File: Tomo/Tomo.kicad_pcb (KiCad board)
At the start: 2 copper layers, 35.6 x 55.9 mm, 60 parts, among them J001 USB_MICROB, J002 STANDOFF_GND, J006 USB_MICROB, J101 Raspberry_Pi_1, J102 CONN_01X02, J301 CONN_02X03, J401 CONN_01X04, U001 FT232RL, U301 ADuM3221, U401 ATMEGA328P-AU, U501 MPU9250, U601 FGPMMOPA6H, U701 HMC5883L, U801 BMP180, U901 L3G4200D, X611 uFL, Y407 16MHz

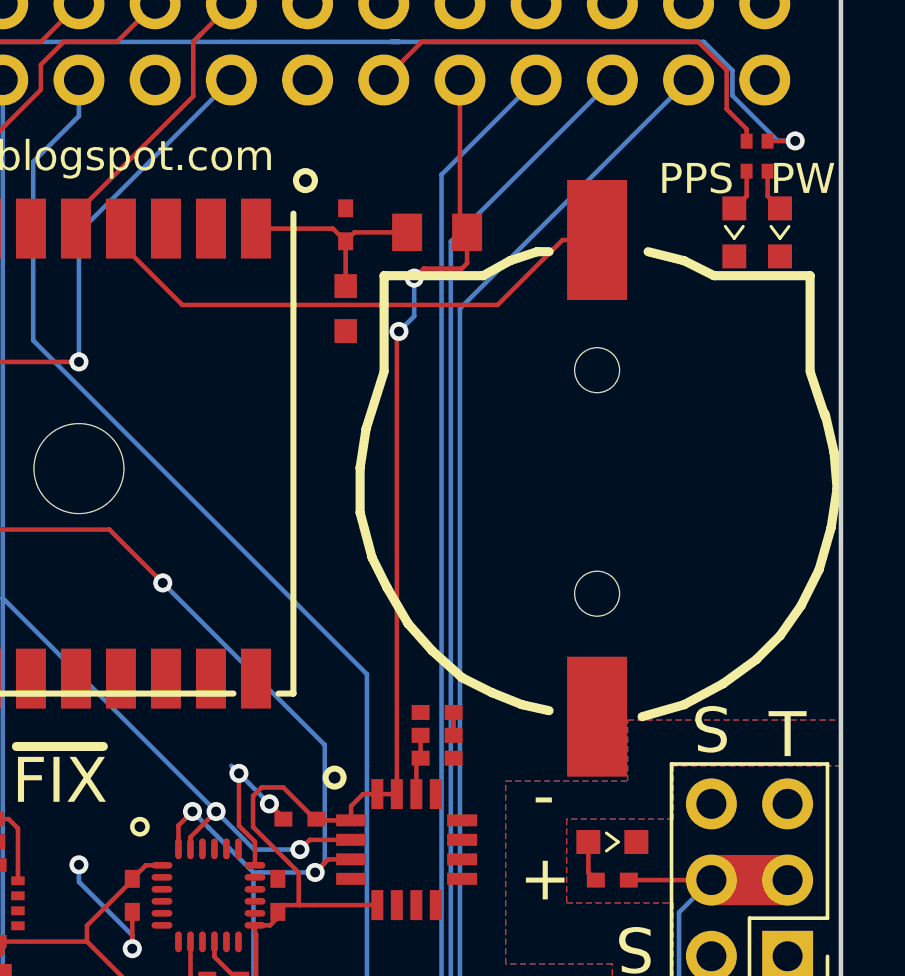
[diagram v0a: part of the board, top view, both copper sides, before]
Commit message: Adding supercap
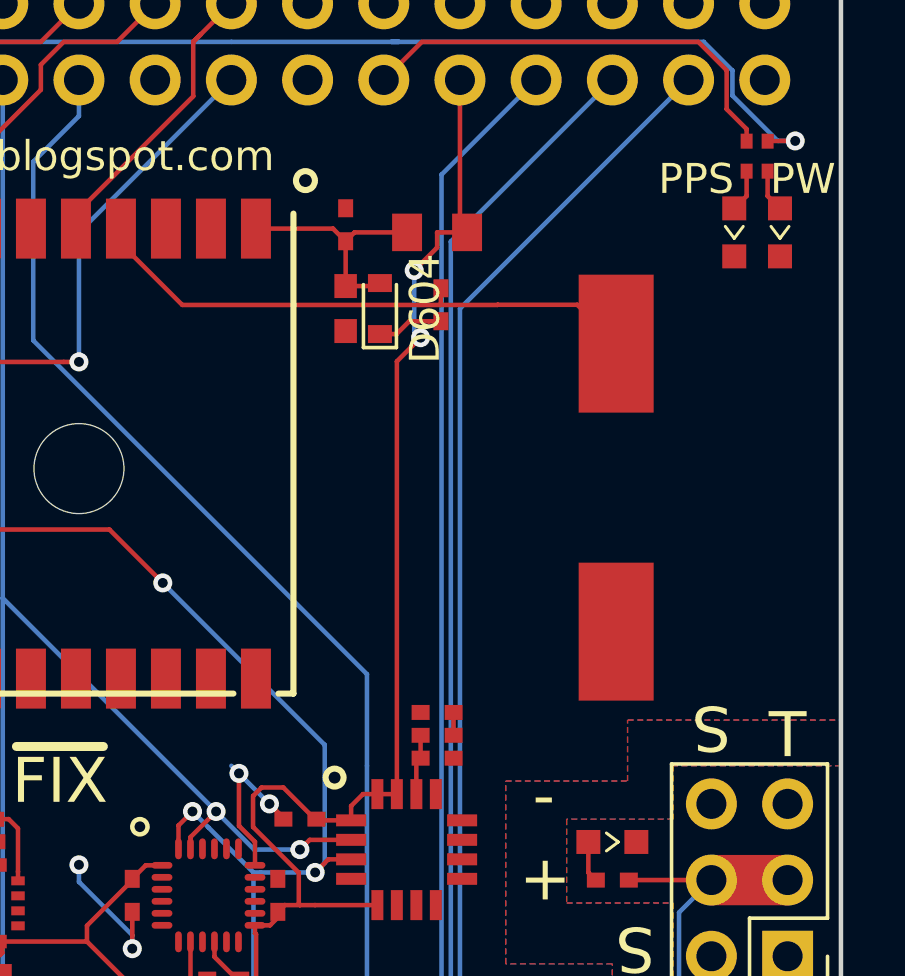
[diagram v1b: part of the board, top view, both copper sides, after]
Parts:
- removed B603: Coin_Cell, KwanSystems:CR1220-2
- added C604: 220mF, KwanSystems:Supercap, F.Cu at (154.6, 117.3)
- added D604: D_Schottky, Diodes_SMD:D_0603, F.Cu at (146.7, 111.3)
- added R604: 10k, KwanSystems:SMD_0402, F.Cu at (148.7, 111.2)
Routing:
- net Net-(D604-Pad1): track 0.00 -> 2.21 mm
- net /VGPS: track 6.83 -> 8.01 mm
- net /VBACKUP: track 18.1 -> 18.9 mm

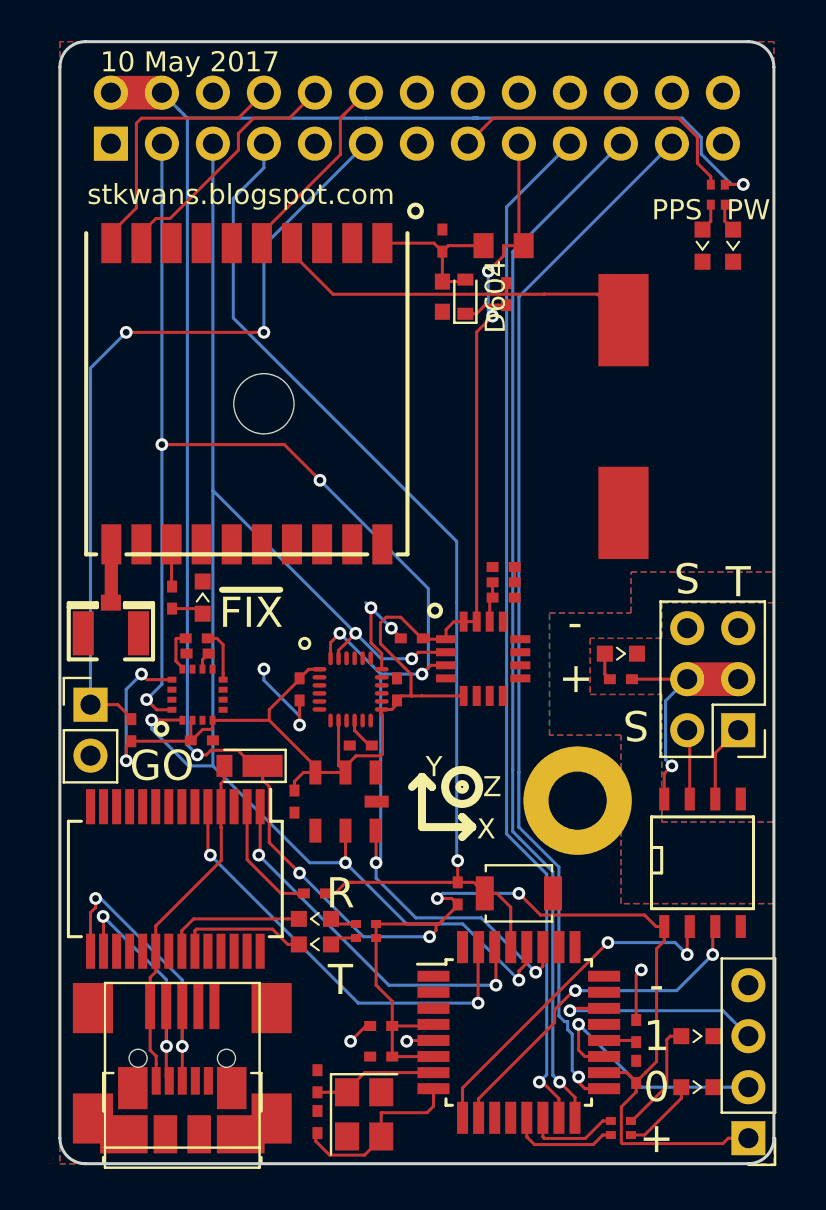
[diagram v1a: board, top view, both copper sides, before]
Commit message: Broke the schematic down to a bunch of subsheets
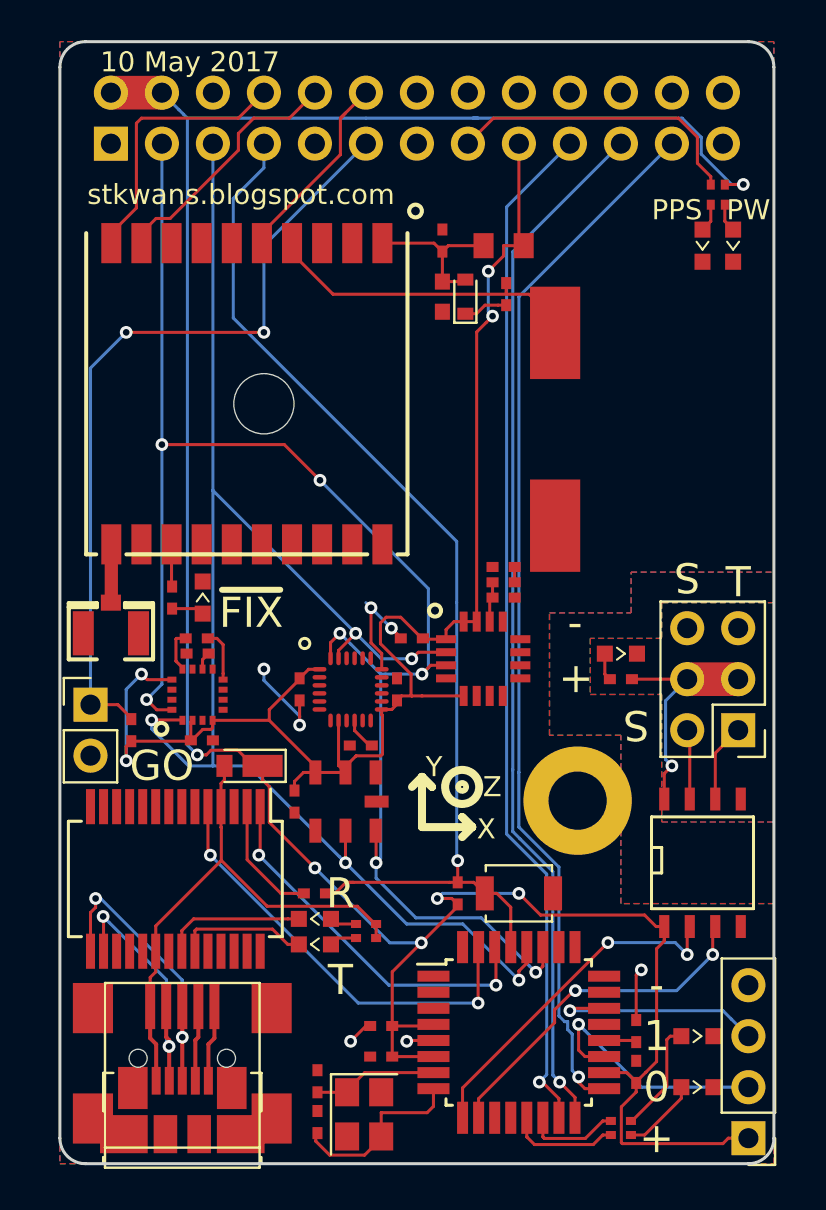
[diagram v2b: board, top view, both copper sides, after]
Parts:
- removed J006: USB_MICROB, KwanSystems:USB_Mini-B
- J001: footprint KwanSystems:USB_Micro-B_Molex_47346-0001 -> KwanSystems:USB_Double-B
- moved C604 3.46 mm to (151.2, 117.9)
- moved J001 2.79 mm to (132.6, 154.5)
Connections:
- net /ANT renamed /UltimateGPS/ANT
- net /AREF renamed /Arduino/AREF
- net /C1 renamed /HMC5883L/C1
- net /D+ renamed /Arduino/D+
- net /D- renamed /Arduino/D-
- net /D0/RX renamed /Arduino/D0
- net /D1/TX renamed /Arduino/D1
- net /DTR renamed /Arduino/DTR
- net /PLLFILT renamed /L3G4200D/PLLFILT
- net /PLLFILT- renamed /L3G4200D/PLLFILT-
- net /RXLED renamed /Arduino/RXLED
- net /RXLED+ renamed /Arduino/RXLED+
- net /SETC renamed /HMC5883L/SETC
- net /SETP renamed /HMC5883L/SETP
- net /TXLED renamed /Arduino/TXLED
- net /TXLED+ renamed /Arduino/TXLED+
- net /VBACKUP renamed /UltimateGPS/VBACKUP
- net /VGPS renamed /UltimateGPS/VGPS
- net /XTAL1 renamed /Arduino/XTAL1
- net /XTAL2 renamed /Arduino/XTAL2
- J001 pad 4: (no net) -> Net-(J001-Pad4)
- J101 pad 1: (no net) -> Net-(J101-Pad1)
- J101 pad 13: (no net) -> Net-(J101-Pad13)
- J101 pad 16: (no net) -> Net-(J101-Pad16)
- J101 pad 18: (no net) -> Net-(J101-Pad18)
- J101 pad 22: (no net) -> Net-(J101-Pad22)
- J101 pad 24: (no net) -> Net-(J101-Pad24)
- J101 pad 26: (no net) -> Net-(J101-Pad26)
- R022 pad 1: +5V -> /VBUS
- R022 pad 2: +5V -> /VBUS
- U001 pad 10: (no net) -> Net-(U001-Pad10)
- U001 pad 11: (no net) -> Net-(U001-Pad11)
- U001 pad 12: (no net) -> Net-(U001-Pad12)
- U001 pad 13: (no net) -> Net-(U001-Pad13)
- U001 pad 14: (no net) -> Net-(U001-Pad14)
- U001 pad 17: (no net) -> Net-(U001-Pad17)
- U001 pad 19: (no net) -> Net-(U001-Pad19)
- U001 pad 27: (no net) -> Net-(U001-Pad27)
- U001 pad 28: (no net) -> Net-(U001-Pad28)
- U001 pad 3: (no net) -> Net-(U001-Pad3)
- U001 pad 6: (no net) -> Net-(U001-Pad6)
- U001 pad 9: (no net) -> Net-(U001-Pad9)
- U401 pad 1: (no net) -> /Arduino/D3
- U401 pad 11: (no net) -> /Arduino/D7
- U401 pad 12: (no net) -> /Arduino/D8
- U401 pad 2: (no net) -> /Arduino/D4
- U401 pad 23: (no net) -> /Arduino/A0
- U401 pad 24: (no net) -> /Arduino/A1
- U401 pad 25: (no net) -> /Arduino/A2
- U401 pad 26: (no net) -> /Arduino/A3
- U401 pad 32: (no net) -> /Arduino/D2
- U501 pad 11: (no net) -> Net-(U501-Pad11)
- U501 pad 12: (no net) -> Net-(U501-Pad12)
- U501 pad 7: (no net) -> Net-(U501-Pad7)
- U601 pad 14: (no net) -> Net-(U601-Pad14)
- U601 pad 2: (no net) -> Net-(U601-Pad2)
- U701 pad 15: (no net) -> Net-(U701-Pad15)
- U901 pad 6: (no net) -> Net-(U901-Pad6)
- U901 pad 7: (no net) -> Net-(U901-Pad7)
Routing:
- net /VBUS: track 17.4 -> 27.1 mm
- net +5V: track 134.4 -> 130.1 mm
- net Net-(J001-Pad4): track 0.00 -> 3.78 mm
- net /UltimateGPS/VBACKUP: track 18.9 -> 17.3 mm

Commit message: j
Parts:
- added B604: Coin_Cell, KwanSystems:CR1220-2, F.Cu at (154.1, 117.4)
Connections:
- J101 pad 1: Net-(J101-Pad1) -> (no net)
- J101 pad 13: Net-(J101-Pad13) -> (no net)
- J101 pad 16: Net-(J101-Pad16) -> (no net)
- J101 pad 18: Net-(J101-Pad18) -> (no net)
- J101 pad 22: Net-(J101-Pad22) -> (no net)
- J101 pad 24: Net-(J101-Pad24) -> (no net)
- J101 pad 26: Net-(J101-Pad26) -> (no net)
- U001 pad 10: Net-(U001-Pad10) -> (no net)
- U001 pad 11: Net-(U001-Pad11) -> (no net)
- U001 pad 12: Net-(U001-Pad12) -> (no net)
- U001 pad 13: Net-(U001-Pad13) -> (no net)
- U001 pad 14: Net-(U001-Pad14) -> (no net)
- U001 pad 17: Net-(U001-Pad17) -> (no net)
- U001 pad 19: Net-(U001-Pad19) -> (no net)
- U001 pad 27: Net-(U001-Pad27) -> (no net)
- U001 pad 28: Net-(U001-Pad28) -> (no net)
- U001 pad 3: Net-(U001-Pad3) -> (no net)
- U001 pad 6: Net-(U001-Pad6) -> (no net)
- U001 pad 9: Net-(U001-Pad9) -> (no net)
- U401 pad 1: /Arduino/D3 -> (no net)
- U401 pad 11: /Arduino/D7 -> (no net)
- U401 pad 12: /Arduino/D8 -> (no net)
- U401 pad 2: /Arduino/D4 -> (no net)
- U401 pad 23: /Arduino/A0 -> (no net)
- U401 pad 24: /Arduino/A1 -> (no net)
- U401 pad 25: /Arduino/A2 -> (no net)
- U401 pad 26: /Arduino/A3 -> (no net)
- U401 pad 32: /Arduino/D2 -> (no net)
- U501 pad 11: Net-(U501-Pad11) -> (no net)
- U501 pad 12: Net-(U501-Pad12) -> (no net)
- U501 pad 7: Net-(U501-Pad7) -> (no net)
- U601 pad 14: Net-(U601-Pad14) -> (no net)
- U601 pad 2: Net-(U601-Pad2) -> (no net)
- U701 pad 15: Net-(U701-Pad15) -> (no net)
- U901 pad 6: Net-(U901-Pad6) -> (no net)
- U901 pad 7: Net-(U901-Pad7) -> (no net)
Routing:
- net /UltimateGPS/VBACKUP: track 17.3 -> 23.0 mm

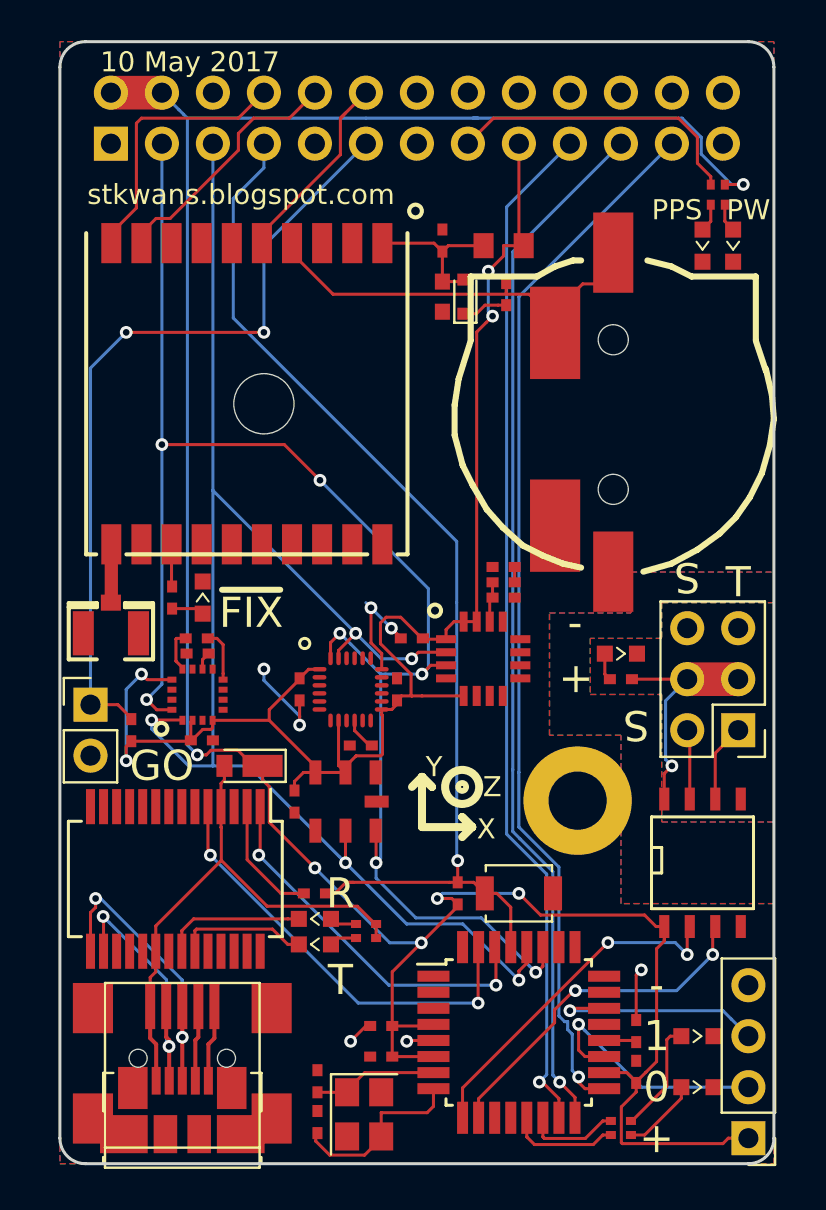
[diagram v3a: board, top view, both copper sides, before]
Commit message: Broke Arduino into ATMega part. Fixed PPS and FIX pins
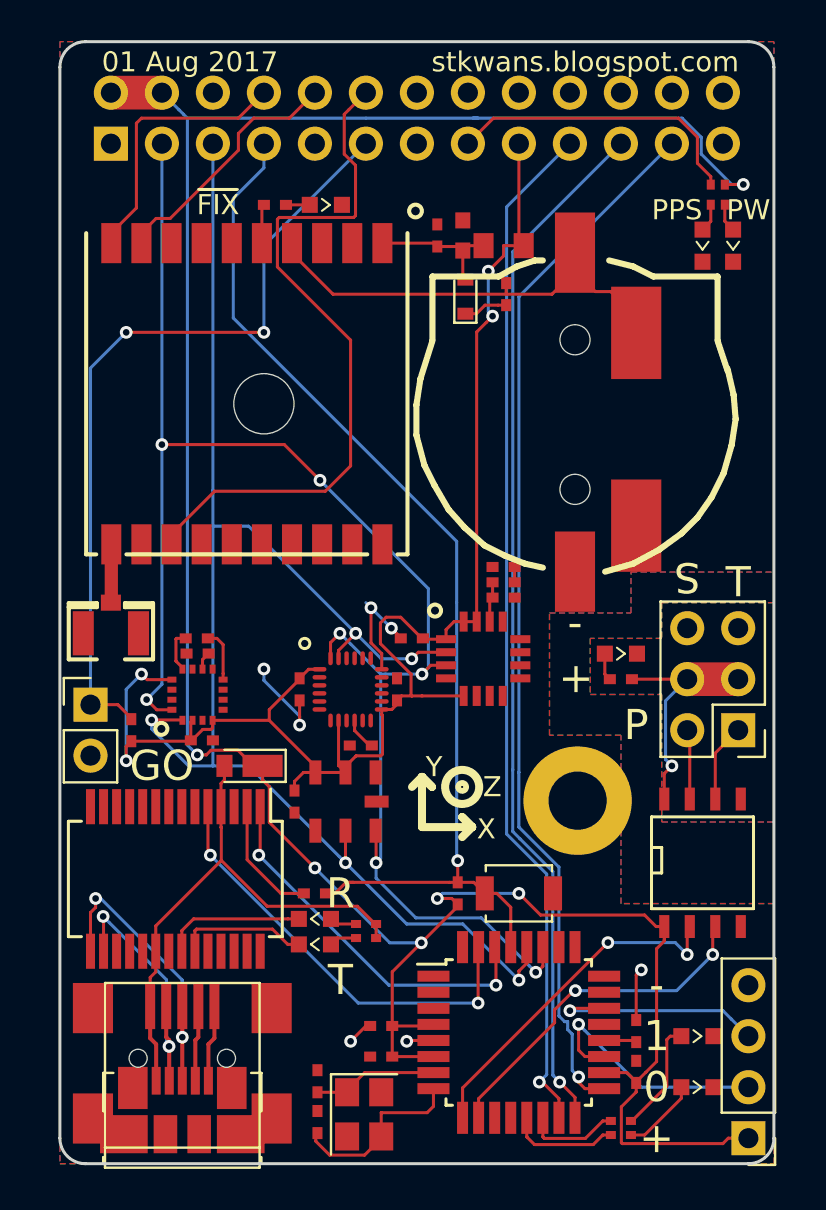
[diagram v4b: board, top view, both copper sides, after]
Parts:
- moved D613 20.5 mm to (139.7, 106.7), turned to 180 degrees
- moved R613 20.2 mm to (137.2, 106.7), turned to 0 degrees
- moved C604 4.04 mm to (155.2, 117.9)
- moved C603 3.21 mm to (146.6, 108.3), turned to 270 degrees
- moved B604 1.91 mm to (152.2, 117.4)
- moved C601 0.36 mm to (145.3, 108.3)
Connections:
- net /Arduino/AREF renamed /Arduino/ATMega/AREF
- net /Arduino/XTAL1 renamed /Arduino/ATMega/XTAL1
- net /Arduino/XTAL2 renamed /Arduino/ATMega/XTAL2
- net /VBUS renamed /Arduino/VBUS
- net Net-(D604-Pad1) renamed /UltimateGPS/VBACKUP+
- U501 pad 20: GND -> (no net)
- U601 pad 13: /FIX -> /PPS
- U601 pad 5: /PPS -> /FIX
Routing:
- net /PPS: track 10.00 -> 35.4 mm
- net /UltimateGPS/VGPS: track 8.01 -> 6.97 mm
- net /UltimateGPS/VBACKUP: track 23.0 -> 22.2 mm
- net /SCL: track 76.7 -> 75.9 mm
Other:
- board text added: "01 Aug 2017"
- board text added: "P"
- board text removed: "10 May 2017"

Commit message: Consistentized the Naninator, Tomo, and Tomo Plugin
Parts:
- D001: value MSS1P6 -> MSS1P2
- U401: footprint Housings_QFP:TQFP-32_7x7mm_Pitch0.8mm -> Housings_QFP:LQFP-32_7x7mm_Pitch0.8mm
- Y407: footprint Crystals:Crystal_SMD_Abracon_ABM8G-4pin_3.2x2.5mm -> Crystals:Crystal_SMD_2520-4pin_2.5x2.0mm
- moved C407 3.40 mm to (142.5, 149.2), turned to 0 degrees
- moved C408 2.76 mm to (142.0, 153.0), turned to 180 degrees
- moved Y407 1.26 mm to (142.1, 150.9), turned to 180 degrees
- moved C406 0.76 mm to (142.5, 148.4)
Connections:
- net /Arduino/ATMega/AREF renamed /Arduino/AREF
- J401 pad 2: /ENCODER0 -> /ENCODER1
- J401 pad 3: /ENCODER1 -> /ENCODER0
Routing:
- net /Arduino/ATMega/XTAL2: track 10.1 -> 6.50 mm
- net /Arduino/ATMega/XTAL1: track 6.33 -> 3.22 mm
- net /ENCODER0: track 12.4 -> 10.5 mm
- net /ENCODER1: track 11.2 -> 12.5 mm, vias 1 -> 2
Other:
- board text added: "github.com/kwan3217"
- board text removed: "stkwans.blogspot.com"

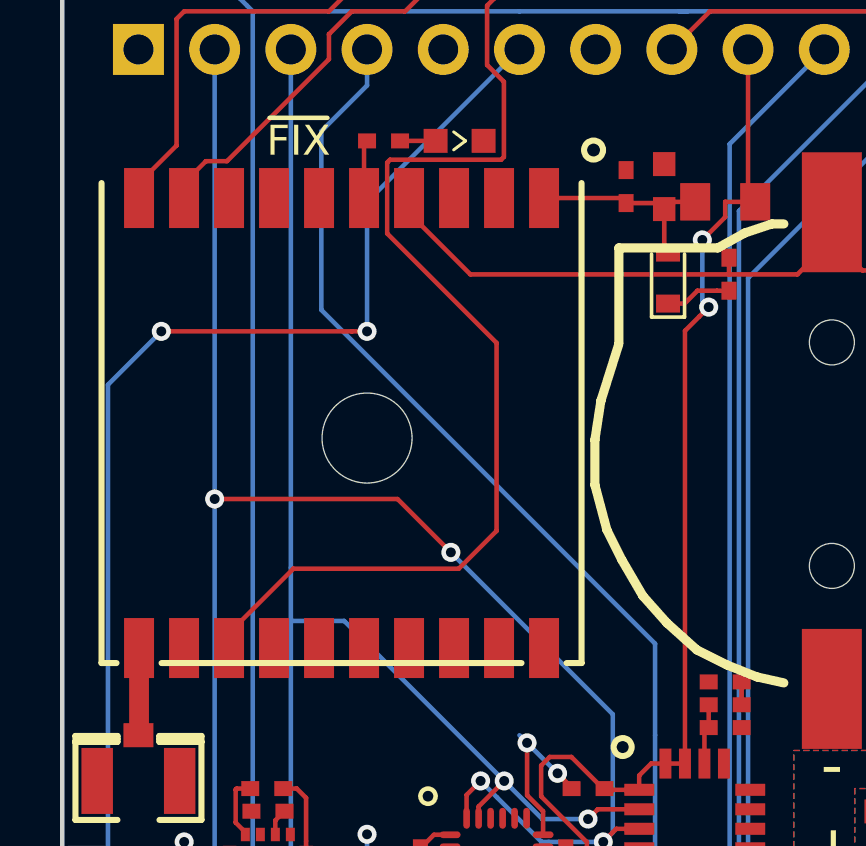
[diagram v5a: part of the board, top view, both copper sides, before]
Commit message: Removed some extraneous silkscreen, changed some footprints to KwanSystems library
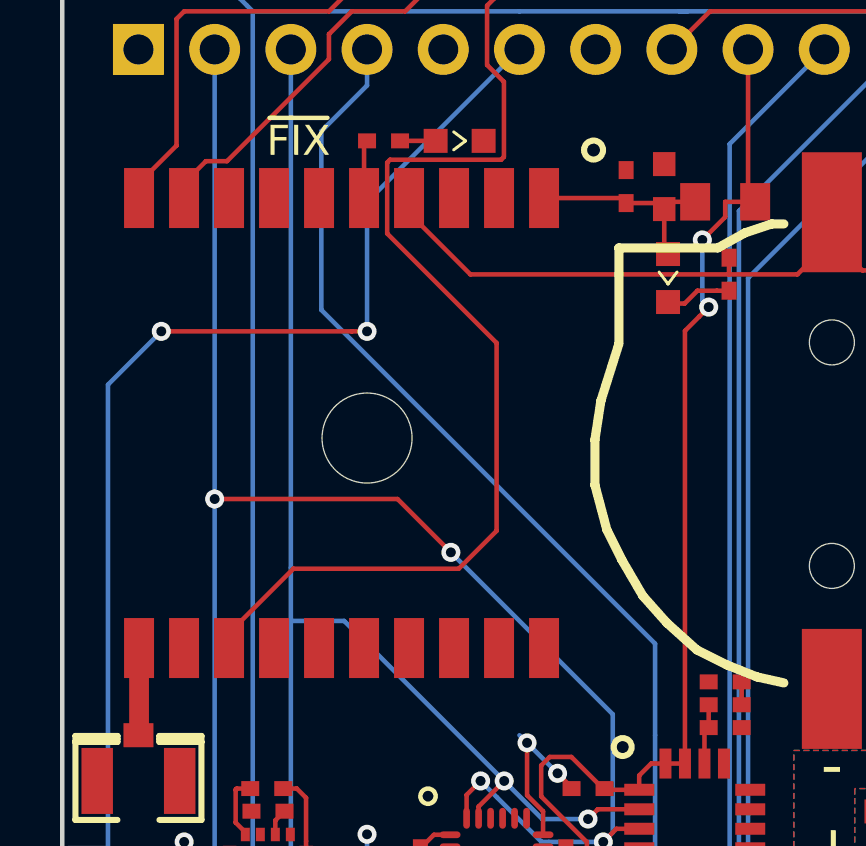
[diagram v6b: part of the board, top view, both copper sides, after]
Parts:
- D604: footprint Diodes_SMD:D_0603 -> KwanSystems:D_0603
- U601: footprint KwanSystems:FGPMMOPA6H -> FGPMMOPA6H

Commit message: Adding kwire stuff
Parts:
- U601: footprint FGPMMOPA6H -> KwanSystems:FGPMMOPA6H
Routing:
- net /ENCODER1: track 12.5 -> 15.2 mm
